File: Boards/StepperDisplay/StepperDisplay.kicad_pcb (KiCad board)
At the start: 2 copper layers, 94 parts, among them IC1 ATTINY861-P, Q1 BC857, Q10 BC857, Q11 BC857, Q12 BC857, Q13 BC857, Q14 BC857, Q15 BC857, Q16 BC857, Q17 BC857, Q18 BC857, Q2 BC857, Q3 BC857, Q4 BC857, Q5 BC857, Q6 BC857, Q7 BC857, Q8 BC857, Q9 BC857, U1 74HC595, U2 74HC595, U3 ULN2801A, U4 74HC595, U5 74HC595, U6 ULN2801A, U7 74HC595, U8 74HC595, U9 ULN2801A

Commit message: Work in Progress
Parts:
- moved R37 118.1 mm to (165.1, 121.9), turned to 90 degrees
- moved R38 113.5 mm to (167.6, 121.9), turned to 90 degrees
- moved R40 113.4 mm to (162.6, 104.6), turned to 270 degrees
- moved R39 110.1 mm to (170.2, 121.9), turned to 90 degrees
- moved R35 108.7 mm to (162.6, 121.9), turned to 270 degrees
- moved R36 101.5 mm to (162.6, 116.8), turned to 270 degrees
- moved R42 99.6 mm to (168.1, 101.6), turned to 90 degrees
- moved R41 94.0 mm to (162.6, 109.7), turned to 270 degrees
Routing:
- net /LEDsY/R_Clock: track 0.00 -> 118.7 mm, vias 0 -> 2
- net /Controller/Ser_Clock: track 125.0 -> 243.3 mm
- net Net-(U4-Pad9): track 0.00 -> 112.6 mm
- net Net-(R34-Pad2): track 0.00 -> 83.0 mm
- net Net-(R33-Pad2): track 0.00 -> 72.2 mm
- net Net-(R32-Pad2): track 0.42 -> 61.2 mm
- net Net-(R31-Pad2): track 0.00 -> 49.3 mm
- net Net-(R30-Pad2): track 0.27 -> 38.2 mm
- net Net-(R29-Pad2): track 0.00 -> 24.6 mm
- net +5V: track 208.4 -> 222.8 mm
- net Net-(Q16-Pad1): track 0.00 -> 9.34 mm
- net Net-(Q15-Pad1): track 0.00 -> 8.30 mm
- net Net-(Q17-Pad1): track 0.00 -> 6.72 mm
- net Net-(Q14-Pad1): track 0.00 -> 6.72 mm
- net Net-(Q18-Pad1): track 0.00 -> 6.61 mm
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
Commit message: Recover from damaged repository
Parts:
- added BZ1: buzzer, Buzzers_Beepers:Buzzer_12x9.5RM7.6, F.Cu at (179.6, 128.5)
- added C10: 100nF, Capacitors_SMD:C_0805_HandSoldering, F.Cu at (81.3, 57.9)
- added C11: 100nF, Capacitors_SMD:C_0805_HandSoldering, F.Cu at (73.9, 57.9)
- added C12: 100µF, Capacitors_SMD:c_elec_4x5.8, F.Cu at (78.0, 106.9)
- added C13: 100nF, Capacitors_SMD:C_0805_HandSoldering, F.Cu at (73.7, 87.1)
- added C14: 100nF, Capacitors_SMD:C_0805_HandSoldering, F.Cu at (81.3, 87.1)
- added C15: 100µF, Capacitors_SMD:c_elec_4x5.8, F.Cu at (94.0, 128.3)
- added C16: 100nF, Capacitors_SMD:C_0805_HandSoldering, F.Cu at (73.9, 114.3)
- added C17: 100nF, Capacitors_SMD:C_0805_HandSoldering, F.Cu at (81.3, 114.3)
- added C18: 100µF, Capacitors_SMD:c_elec_4x5.8, F.Cu at (78.0, 77.7)
- added C7: 100nF, Capacitors_SMD:C_0805, F.Cu at (122.2, 132.3)
- added C8: 100nF, Capacitors_SMD:C_0805, F.Cu at (141.0, 133.9)
- added C9: 100µF, Capacitors_SMD:c_elec_4x5.8, F.Cu at (77.7, 49.0)
- added P1: CONN_01X06, Pin_Headers:Pin_Header_Angled_2x03, F.Cu at (94.0, 134.9)
- added P2: ISP, Pin_Headers:Pin_Header_Angled_2x03, F.Cu at (107.4, 134.9)
- added SW1: SW_PUSH, Buttons_Switches_SMD:SW_SPST_EVPBF, F.Cu at (150.6, 134.1)
- added SW2: SW_PUSH, Buttons_Switches_SMD:SW_SPST_EVPBF, F.Cu at (166.6, 134.1)
- added X1: CRYSTAL_SMD, Crystals:Resonator_7.2x3mm, F.Cu at (116.1, 134.4)
- C1, C3, C6, R36, R38, R40, R42: moved to B.Cu
- moved C6 100.2 mm to (181.4, 107.2)
- moved C3 95.1 mm to (176.0, 74.4)
- moved C1 95.1 mm to (176.0, 45.5)
- moved IC1 86.1 mm to (132.1, 133.1), turned to 270 degrees
- moved R42 15.3 mm to (162.6, 115.8)
- moved R35 11.7 mm to (162.6, 110.2)
- moved R39 7.64 mm to (162.6, 121.4)
- moved R37 6.60 mm to (162.6, 115.8)
- moved R36 6.60 mm to (162.6, 110.2)
- moved R38 5.11 mm to (162.6, 121.4)
- moved R41 5.08 mm to (162.6, 104.6)
- moved C5 0.51 mm to (177.8, 119.4)
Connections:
- IC1 pad 1: (no net) -> MOSI
- IC1 pad 10: (no net) -> Net-(IC1-Pad10)
- IC1 pad 11: (no net) -> Net-(IC1-Pad11)
- IC1 pad 14: (no net) -> Net-(IC1-Pad14)
- IC1 pad 17: (no net) -> Net-(BZ1-Pad1)
- IC1 pad 2: (no net) -> MISO
- IC1 pad 3: (no net) -> SCK
- IC1 pad 7: (no net) -> Net-(IC1-Pad7)
- IC1 pad 8: (no net) -> Net-(IC1-Pad8)
- IC1 pad 9: (no net) -> CS
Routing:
- net +5V: track 222.8 -> 504.7 mm, vias 0 -> 7
- net /Controller/Ser_Clock: track 243.3 -> 502.4 mm, vias 2 -> 4
- net /LEDsZ/Ser_In: track 0.00 -> 158.3 mm
- net /LEDsY/Ser_In: track 0.00 -> 157.6 mm
- net /LEDsX/Ser_In: track 0.00 -> 146.0 mm, vias 0 -> 1
- net /Controller/Enable: track 0.00 -> 145.7 mm, vias 0 -> 1
- net /LEDsZ/R_Clock: track 0.00 -> 127.5 mm, vias 0 -> 2
- net Net-(U7-Pad9): track 0.00 -> 116.6 mm
- net Net-(AFF13-Pad4): track 0.00 -> 92.2 mm, vias 0 -> 10
- net Net-(AFF13-Pad7): track 18.8 -> 88.9 mm, vias 2 -> 10
- net SCK: track 0.00 -> 53.7 mm
- net CS: track 0.00 -> 49.3 mm
- net MISO: track 0.00 -> 43.8 mm
- net MOSI: track 0.00 -> 42.0 mm
- net Net-(BZ1-Pad1): track 0.00 -> 40.0 mm
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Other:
- board outline added: 120.4 x 102.1 mm

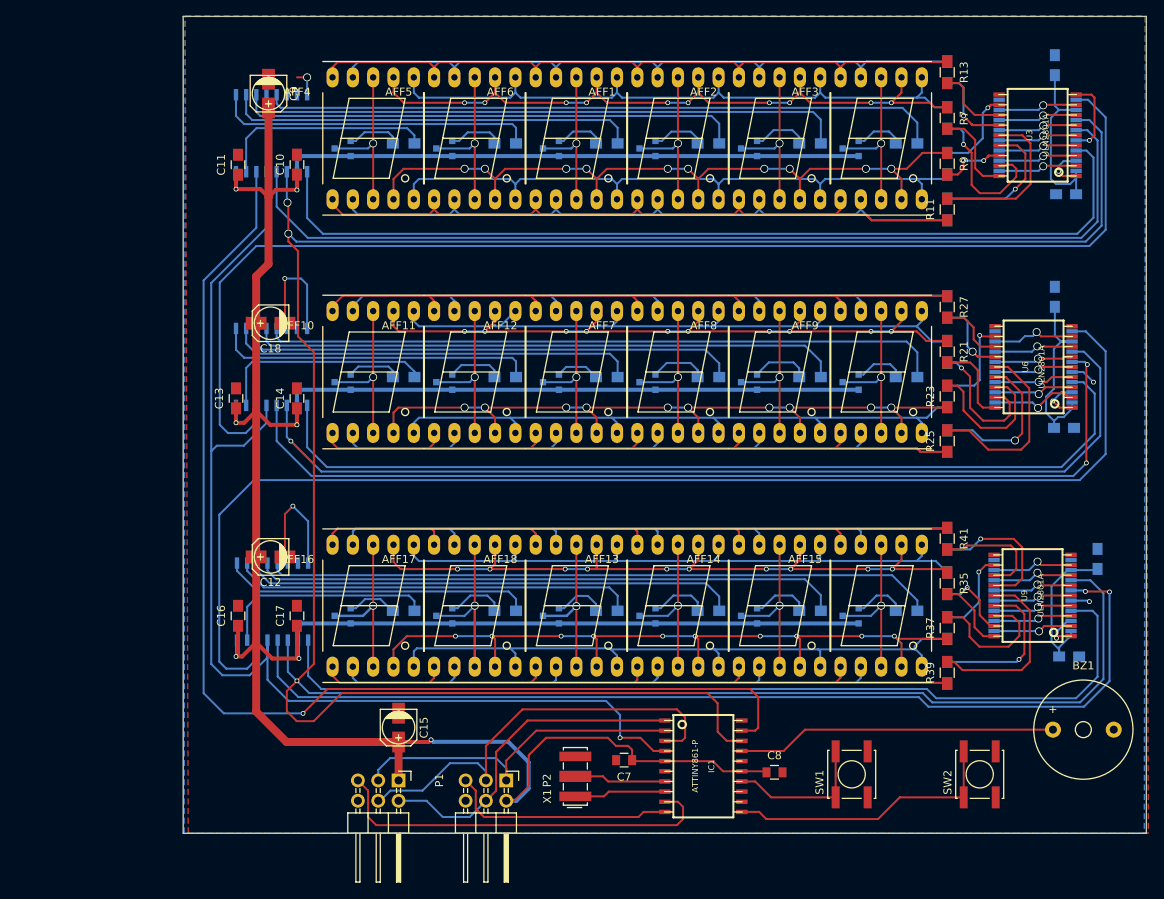
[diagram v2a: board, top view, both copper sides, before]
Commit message: Layout Displayplatine fertig
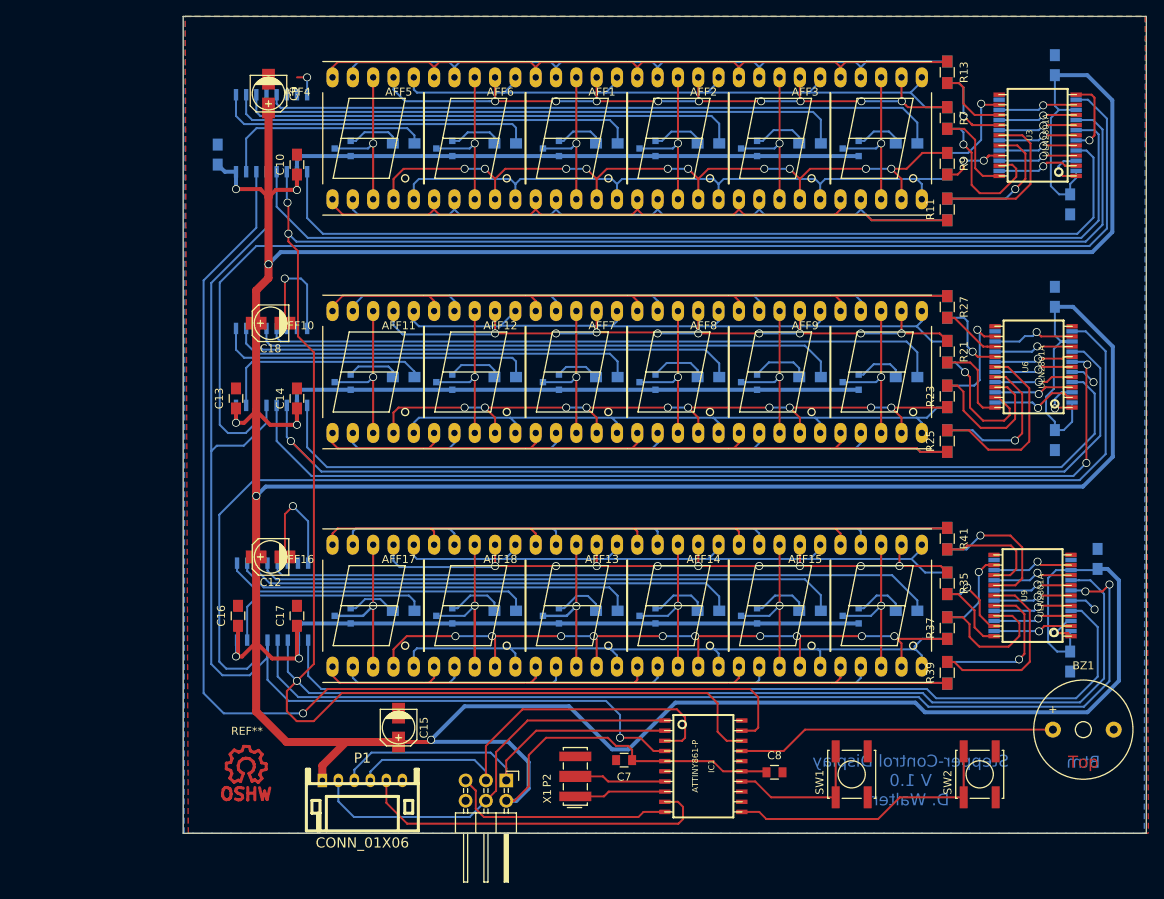
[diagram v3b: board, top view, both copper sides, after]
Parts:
- added REF**: Symbol_OSHW-Logo_CopperTop, Symbols:Symbol_OSHW-Logo_CopperTop, F.Cu at (74.9, 133.1)
- C11: moved to B.Cu
- P1: footprint Pin_Headers:Pin_Header_Angled_2x03 -> w_conn_jst-ph:s6b-ph-kl
- moved P1 4.52 mm to (89.5, 134.9), turned to 0 degrees
- moved C11 2.84 mm to (71.4, 56.6)
- moved C4 1.90 mm to (176.0, 92.3), turned to 270 degrees
- moved C2 1.37 mm to (177.9, 62.9), turned to 270 degrees
- moved C5 0.65 mm to (177.9, 120.0), turned to 270 degrees
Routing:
- net +5V: track 504.7 -> 888.7 mm, vias 7 -> 9
- net MOSI: track 42.0 -> 52.1 mm
- net CS: track 49.3 -> 45.3 mm
- net MISO: track 43.8 -> 47.4 mm
- net Net-(AFF13-Pad7): track 88.9 -> 86.5 mm, vias 10 -> 9
- net Net-(AFF1-Pad6): track 81.9 -> 83.5 mm
- net Net-(R28-Pad2): track 11.9 -> 13.3 mm
- net Net-(AFF10-Pad7): track 87.2 -> 85.9 mm, vias 10 -> 9
- net /LEDsZ/R_Clock: track 127.5 -> 128.7 mm
- net GND: track 47.6 -> 48.6 mm
- net SCK: track 53.7 -> 54.6 mm
- net Net-(R27-Pad2): track 8.37 -> 7.48 mm
- net Net-(U7-Pad9): track 116.6 -> 115.8 mm
- net Net-(AFF1-Pad7): track 87.4 -> 86.7 mm, vias 10 -> 9
- net /LEDsX/R_Clock: track 122.8 -> 123.4 mm
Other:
- board text added: "Btm"
- board text added: "Stepper-Control Display V 1.0 D. Walter"
- board text added: "Top"

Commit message: Layouting...
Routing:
- net GND: track 48.6 -> 57.2 mm, vias 6 -> 7
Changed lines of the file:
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@@
     (links 387)
     (no_connects 0)
-    (area 67.005999 39.319999 187.502001 141.528001)
+    (area 63.155355 39.319999 187.706001 148.299001)
     (thickness 1.6)
     (drawings 8)
-    (tracks 1607)
+    (tracks 1611)
     (zones 0)
     (modules 113)
@@
   )
   (setup
-    (last_trace_width 0.5)
+    (last_trace_width 0.25)
     (user_trace_width 0.3048)
     (user_trace_width 0.5)
@@
   (segment (start 153.380696 53.757842) (end 155.284825 53.757842) (width 0.25) (layer B.Cu) (net 17))
   (segment (start 155.284825 53.757842) (end 156.13 54.603017) (width 0.25) (layer B.Cu) (net 17) (status 20))
+  (segment (start 116.078 131.866) (end 114.678 131.866) (width 0.25) (layer F.Cu) (net 18))
+  (segment (start 114.678 131.866) (end 111.76 134.784) (width 0.25) (layer F.Cu) (net 18))
+  (segment (start 111.76 134.784) (end 111.76 137.795) (width 0.25) (layer F.Cu) (net 18))
+  (via (at 111.76 137.795) (size 0.6) (drill 0.4) (layers F.Cu B.Cu) (net 18))
   (segment (start 178.03876 112.395) (end 179.884071 112.395) (width 0.25) (layer B.Cu) (net 18))
   (segment (start 179.884071 112.395) (end 180.481351 112.99228) (width 0.25) (layer B.Cu) (net 18))
@@
   (via (at 174.5615 55.5625) (size 1) (drill 0.8) (layers F.Cu B.Cu) (net 23))
   (segment (start 173.99 56.134) (end 174.5615 55.5625) (width 0.25) (layer B.Cu) (net 23))
-  (segment (start 178.67376 56.769) (end 174.625 56.769) (width 0.25) (layer F.Cu) (net 24) (status 400000))
+  (segment (start 178.67376 56.769) (end 174.625 56.769) (width 0.25) (layer F.Cu) (net 24))
   (segment (start 174.625 56.769) (end 174.5615 56.8325) (width 0.25) (layer F.Cu) (net 24))
   (segment (start 174.625 56.769) (end 174.5615 56.8325) (width 0.25) (layer F.Cu) (net 24))
@@
   (segment (start 174.5615 56.8325) (end 173.99 57.404) (width 0.25) (layer B.Cu) (net 24))
   (segment (start 173.99 57.404) (end 169.05224 57.404) (width 0.25) (layer B.Cu) (net 24) (status 20))
-  (segment (start 178.67376 58.039) (end 177.292 58.039) (width 0.25) (layer F.Cu) (net 25) (status 400000))
+  (segment (start 178.67376 58.039) (end 177.292 58.039) (width 0.25) (layer F.Cu) (net 25))
   (segment (start 175.006 57.658) (end 174.5615 58.1025) (width 0.25) (layer F.Cu) (net 25))
   (segment (start 176.911 57.658) (end 175.006 57.658) (width 0.25) (layer F.Cu) (net 25))
@@
   (segment (start 129.413 129.921) (end 129.794 129.54) (width 0.25) (layer F.Cu) (net 142))
   (segment (start 92.456 134.874) (end 92.456 137.680914) (width 0.25) (layer F.Cu) (net 143))
-  (segment (start 92.456 137.680914) (end 95.054358 140.279272) (width 0.25) (layer F.Cu) (net 143))
-  (segment (start 129.54 138.176) (end 128.905 137.541) (width 0.25) (layer F.Cu) (net 143))
-  (segment (start 95.054358 140.279272) (end 128.960728 140.279272) (width 0.25) (layer F.Cu) (net 143))
-  (segment (start 128.960728 140.279272) (end 129.54 139.7) (width 0.25) (layer F.Cu) (net 143))
+  (segment (start 92.456 137.680914) (end 94.855179 140.080093) (width 0.25) (layer F.Cu) (net 143))
+  (segment (start 94.855179 140.080093) (end 129.159907 140.080093) (width 0.25) (layer F.Cu) (net 143))
+  (segment (start 129.159907 140.080093) (end 129.54 139.7) (width 0.25) (layer F.Cu) (net 143))
   (segment (start 129.54 139.7) (end 129.54 138.176) (width 0.25) (layer F.Cu) (net 143))
+  (segment (start 129.54 138.176) (end 128.905 137.541) (width 0.25) (layer F.Cu) (net 143))
   (segment (start 128.905 137.541) (end 127.26924 137.541) (width 0.25) (layer F.Cu) (net 143))
   (segment (start 127.26924 138.811) (end 124.603906 138.811) (width 0.25) (layer F.Cu) (net 144) (status 10))

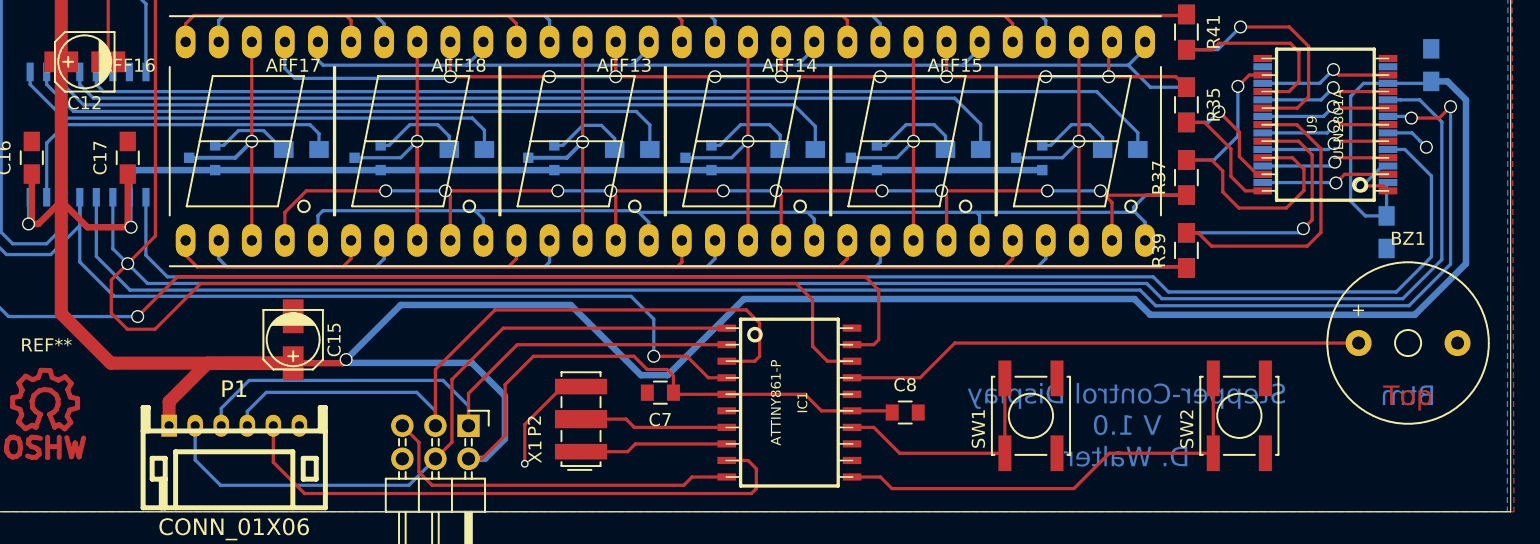
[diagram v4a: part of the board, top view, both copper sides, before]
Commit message: Fixed Part Libraries
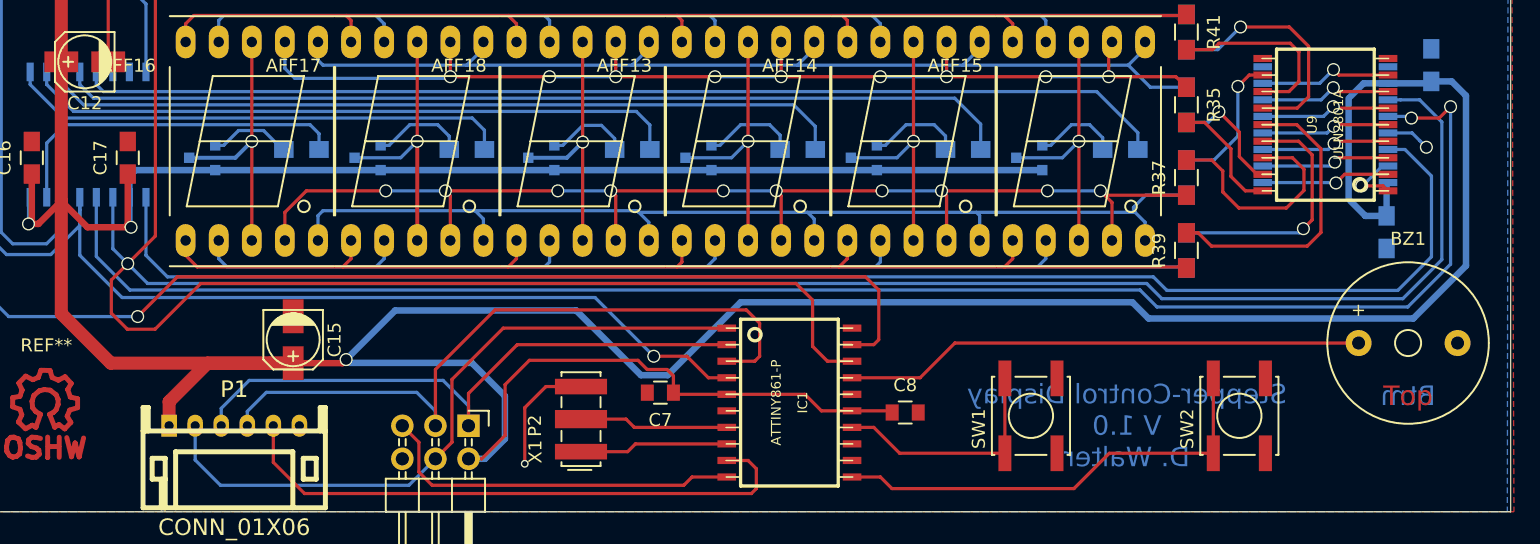
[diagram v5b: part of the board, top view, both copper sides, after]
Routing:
- net /Controller/Enable: track 145.7 -> 143.7 mm
- net GND: track 57.2 -> 57.9 mm
